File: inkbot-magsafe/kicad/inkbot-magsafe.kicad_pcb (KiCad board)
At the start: 4 copper layers, 60 x 99 mm, 70 parts, among them J1 Hirose_FH12-24S-0.5SH_1x24-1M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, J2 Molex_Pico-EZmate_78171-0003_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, J3 Coil_SolderPads, Q1 SOT-323_SC-70, U1 Raytac_MDBT50Q, U2 Texas_VQFN-RHL-20, U3 BQ25185_DLH0010A, U4 SOT-23-5, Y1 Crystal_SMD_3215-2Pin_3.2x1.5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

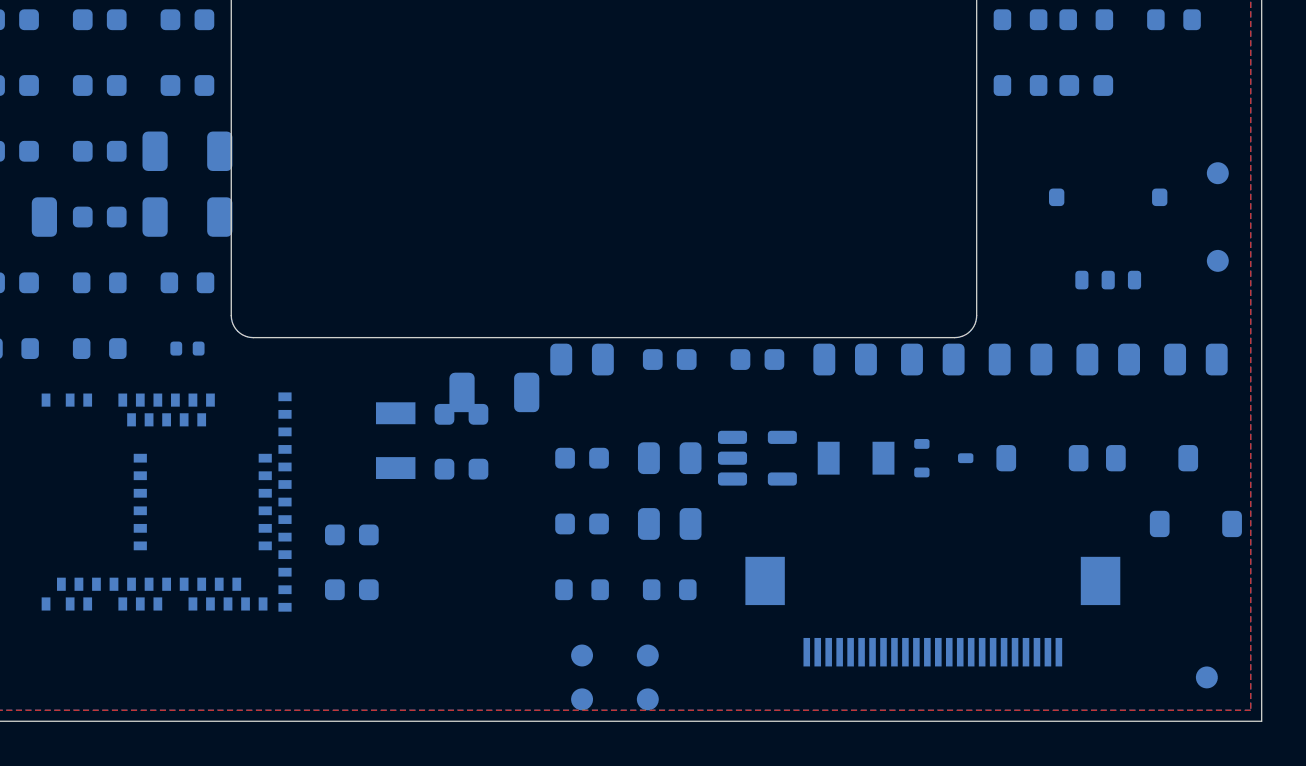
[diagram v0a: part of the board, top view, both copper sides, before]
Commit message: inkbot-magsafe: clear production placement rules
Co-authored-by: Jason Hall <imjasonh@users.noreply.github.com>
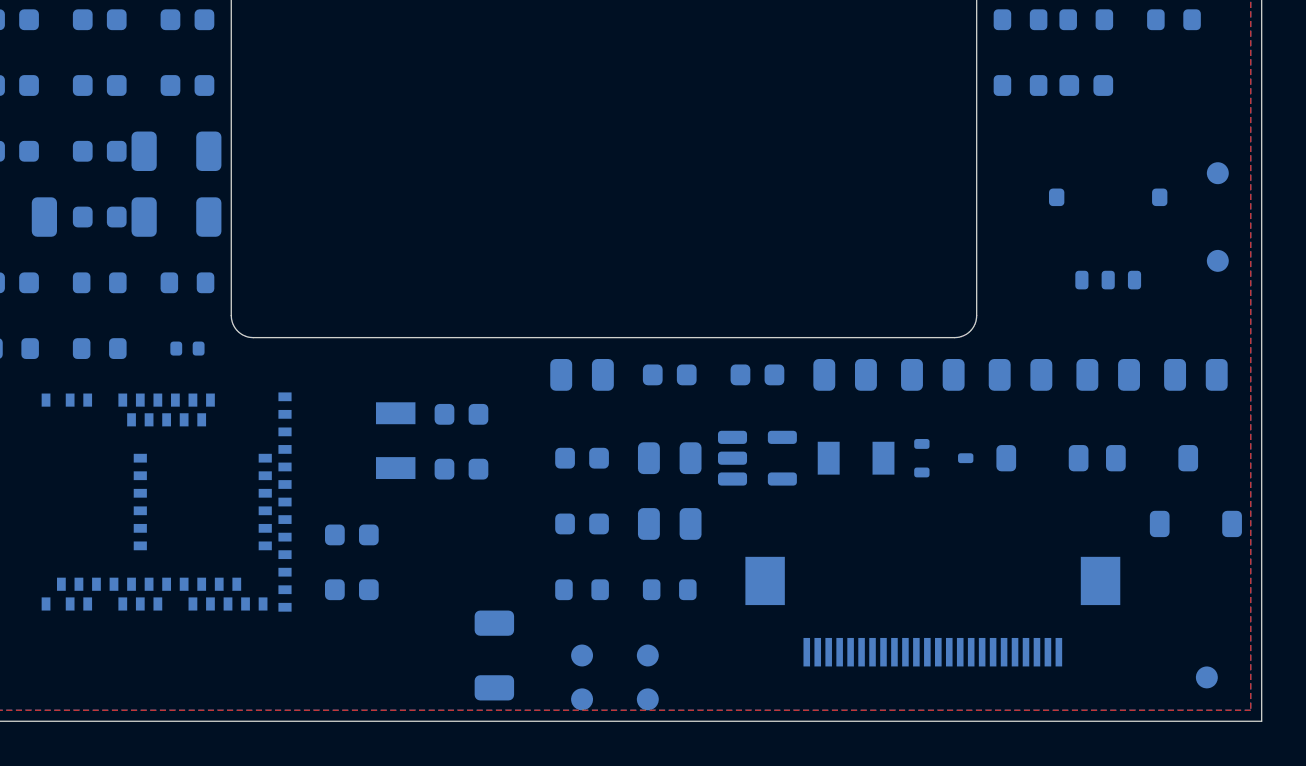
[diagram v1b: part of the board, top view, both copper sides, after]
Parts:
- moved C38 12.0 mm to (25.0, 96.0), turned to -90 degrees
- moved C28 0.70 mm to (29.0, 83.2)
- moved C29 0.70 mm to (33.0, 83.2)
- moved C30 0.70 mm to (37.0, 83.2)
- moved C31 0.70 mm to (41.0, 83.2)
- moved C32 0.70 mm to (45.0, 83.2)
- moved C33 0.70 mm to (49.0, 83.2)
- moved C34 0.70 mm to (53.0, 83.2)
- moved C35 0.70 mm to (57.0, 83.2)
- moved C12 0.50 mm to (10.5, 73.0)
- moved C15 0.50 mm to (10.5, 76.0)

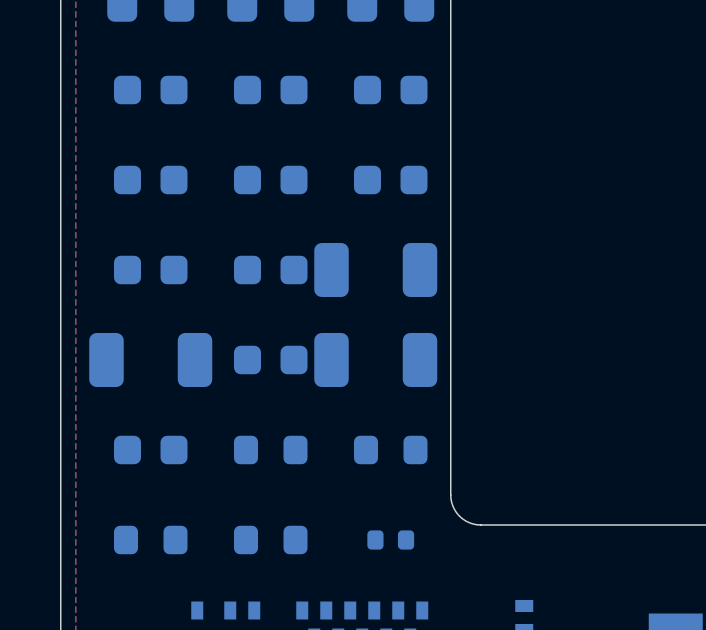
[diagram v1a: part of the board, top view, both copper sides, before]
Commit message: inkbot-magsafe: finish EVT placement clearance
Co-authored-by: Jason Hall <imjasonh@users.noreply.github.com>
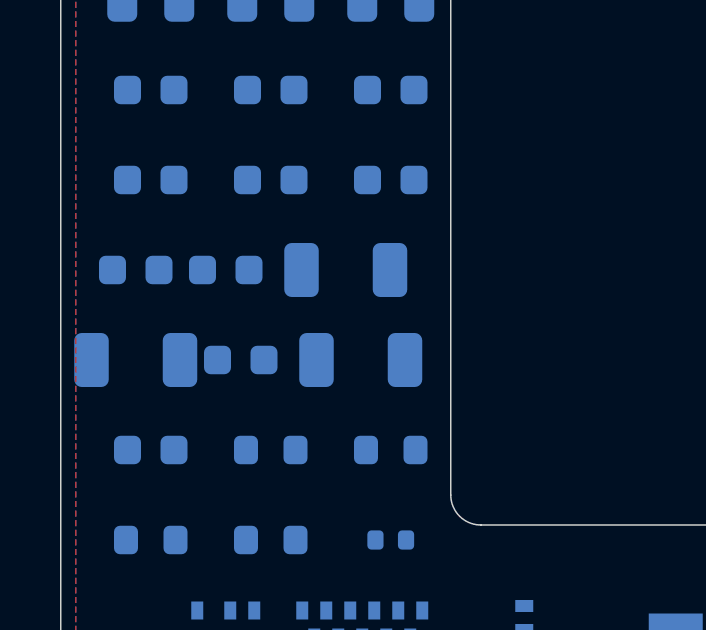
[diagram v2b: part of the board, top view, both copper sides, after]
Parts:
- moved C11 1.50 mm to (5.50, 73.0)
- moved C12 1.00 mm to (9.50, 73.0)
- moved C14 1.00 mm to (6.00, 76.0)
- moved C10 0.50 mm to (2.50, 73.0)
- moved C13 0.50 mm to (2.50, 76.0)
- moved C15 0.50 mm to (10.0, 76.0)

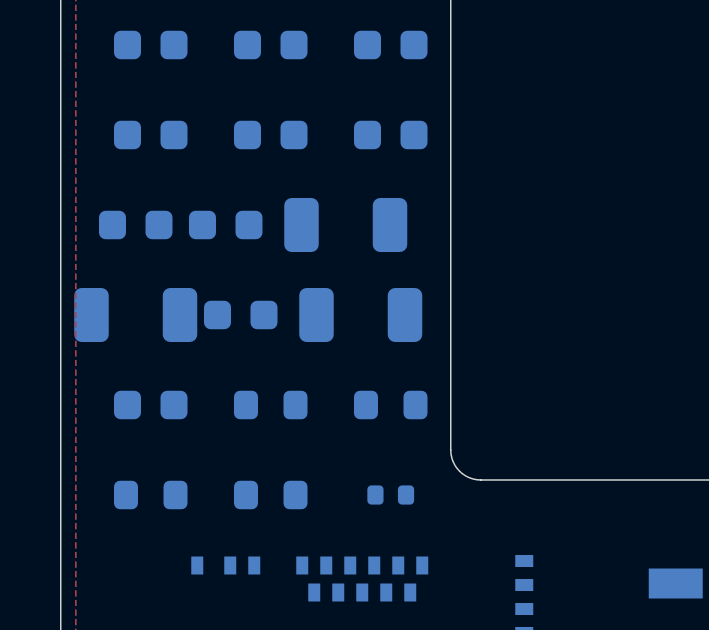
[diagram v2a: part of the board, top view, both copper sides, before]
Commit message: inkbot-magsafe: complete placed-pad contracts
Co-authored-by: Jason Hall <imjasonh@users.noreply.github.com>
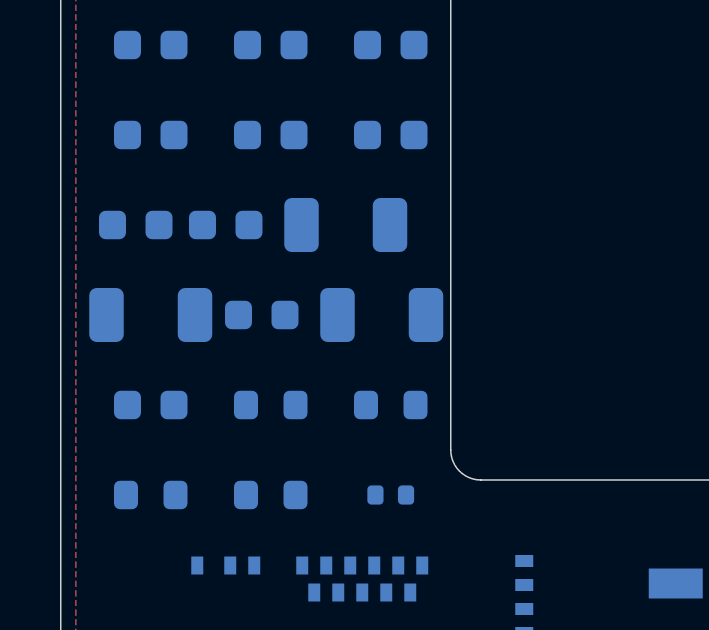
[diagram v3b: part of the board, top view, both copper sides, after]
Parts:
- moved C14 0.70 mm to (6.70, 76.0)
- moved C15 0.70 mm to (10.7, 76.0)
- moved C13 0.50 mm to (3.00, 76.0)

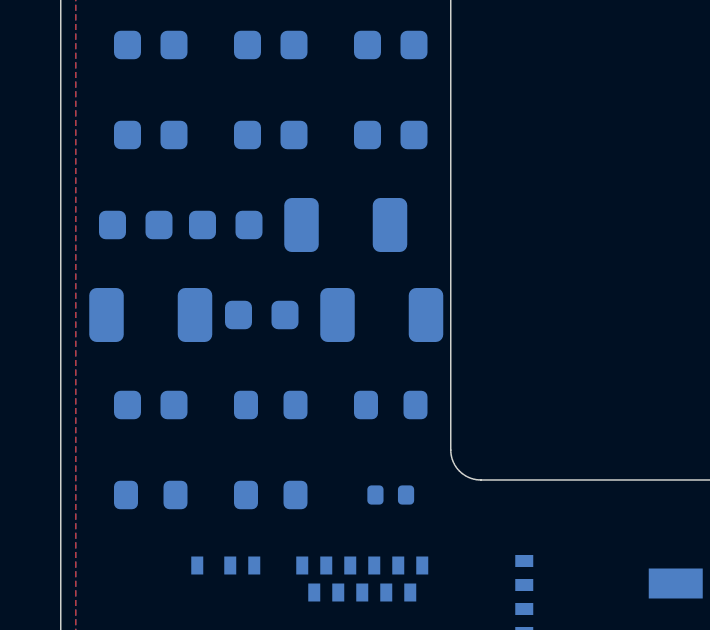
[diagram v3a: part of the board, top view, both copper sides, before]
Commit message: inkbot-magsafe: clear battery-edge placement
Co-authored-by: Jason Hall <imjasonh@users.noreply.github.com>
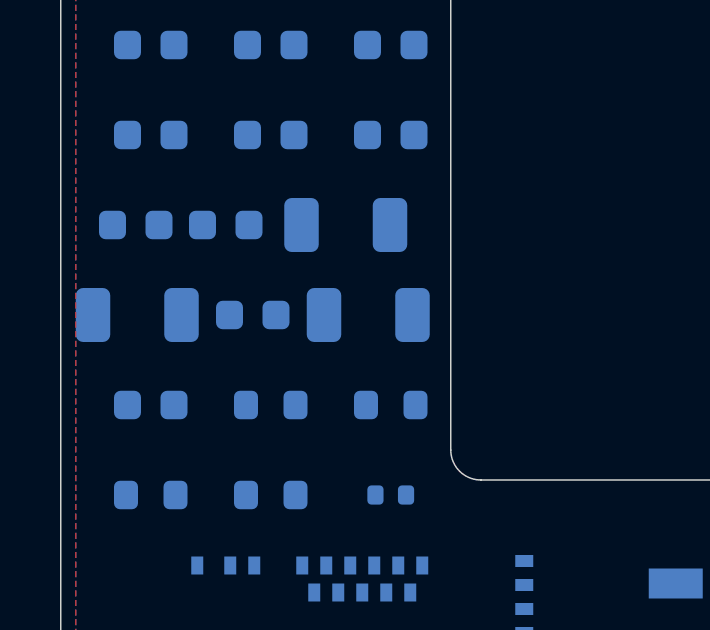
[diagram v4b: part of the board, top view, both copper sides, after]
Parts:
- moved C13 0.45 mm to (2.55, 76.0)
- moved C15 0.45 mm to (10.2, 76.0)
- moved C14 0.30 mm to (6.40, 76.0)

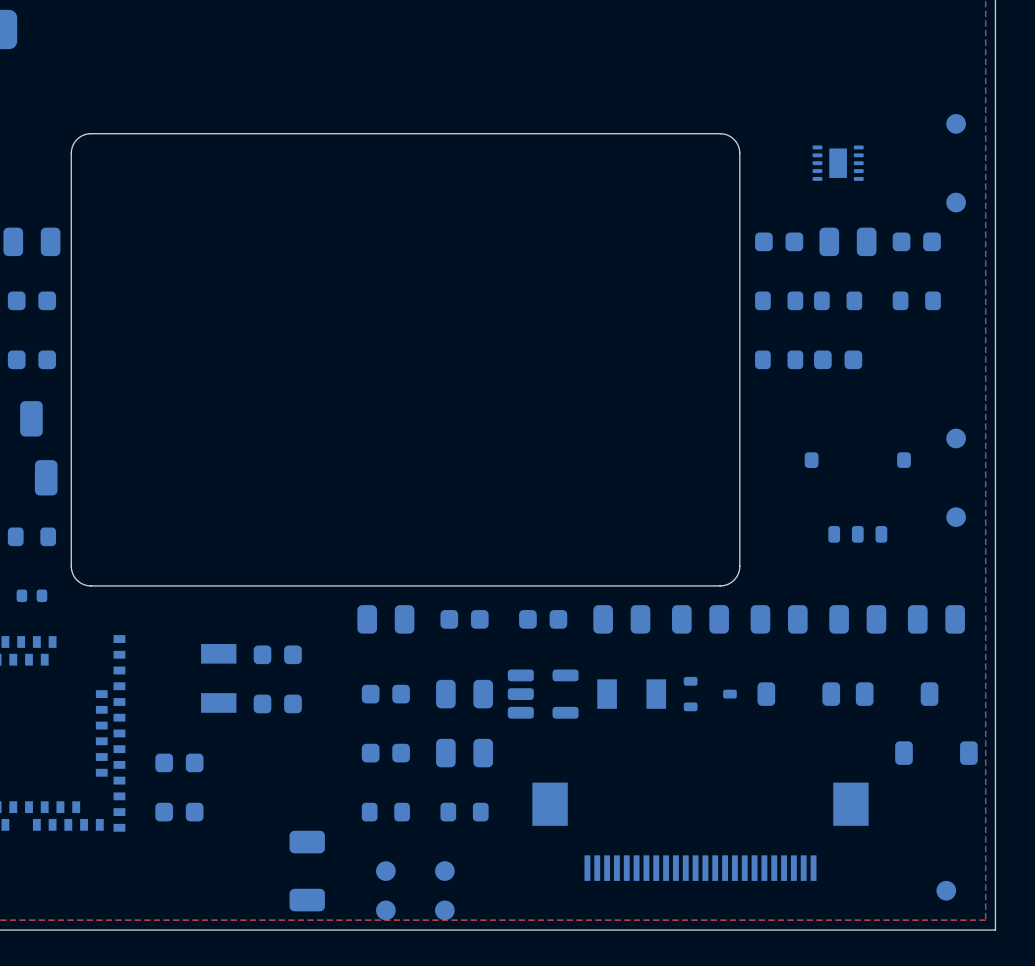
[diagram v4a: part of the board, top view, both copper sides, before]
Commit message: inkbot-magsafe: preconnect power and charge control
Co-authored-by: Jason Hall <imjasonh@users.noreply.github.com>
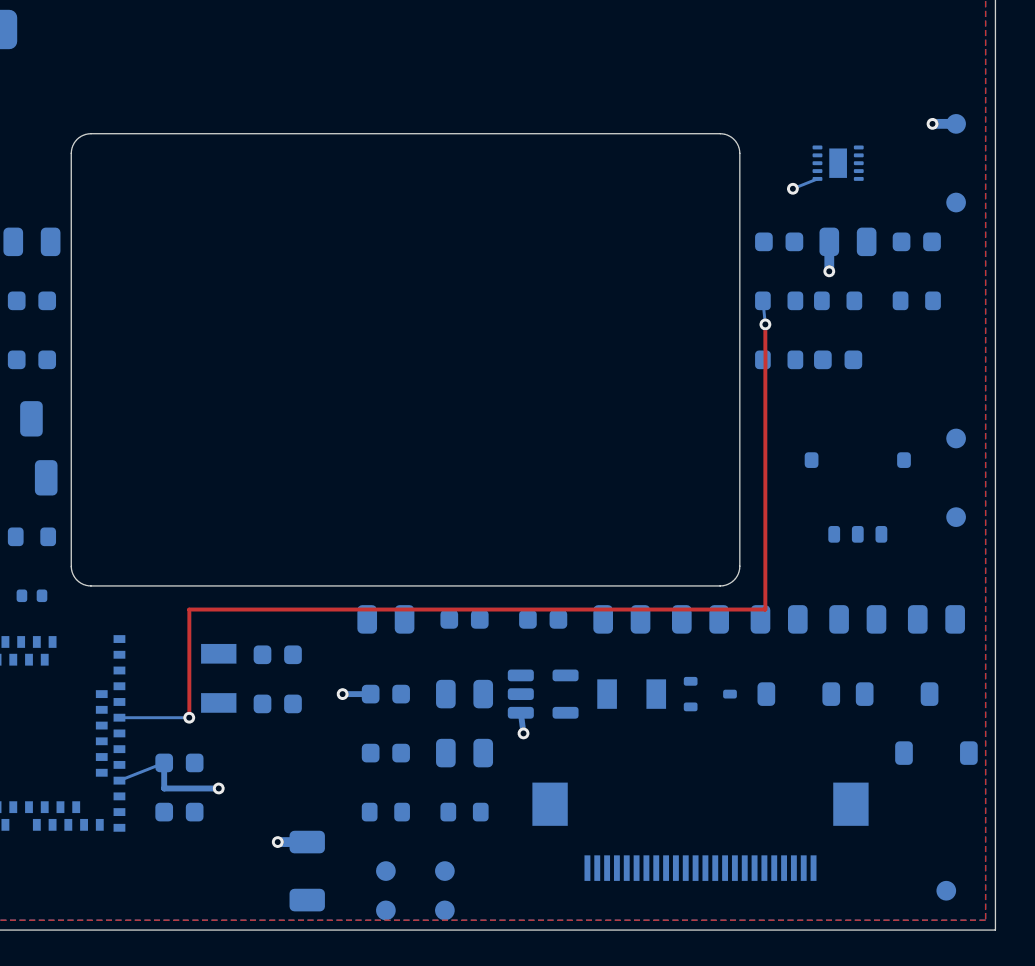
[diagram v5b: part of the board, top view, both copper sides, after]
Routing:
- net /CHG_EN_N: track 0.00 -> 54.1 mm, vias 0 -> 2
- net /SYS: track 0.00 -> 14.6 mm, vias 0 -> 7

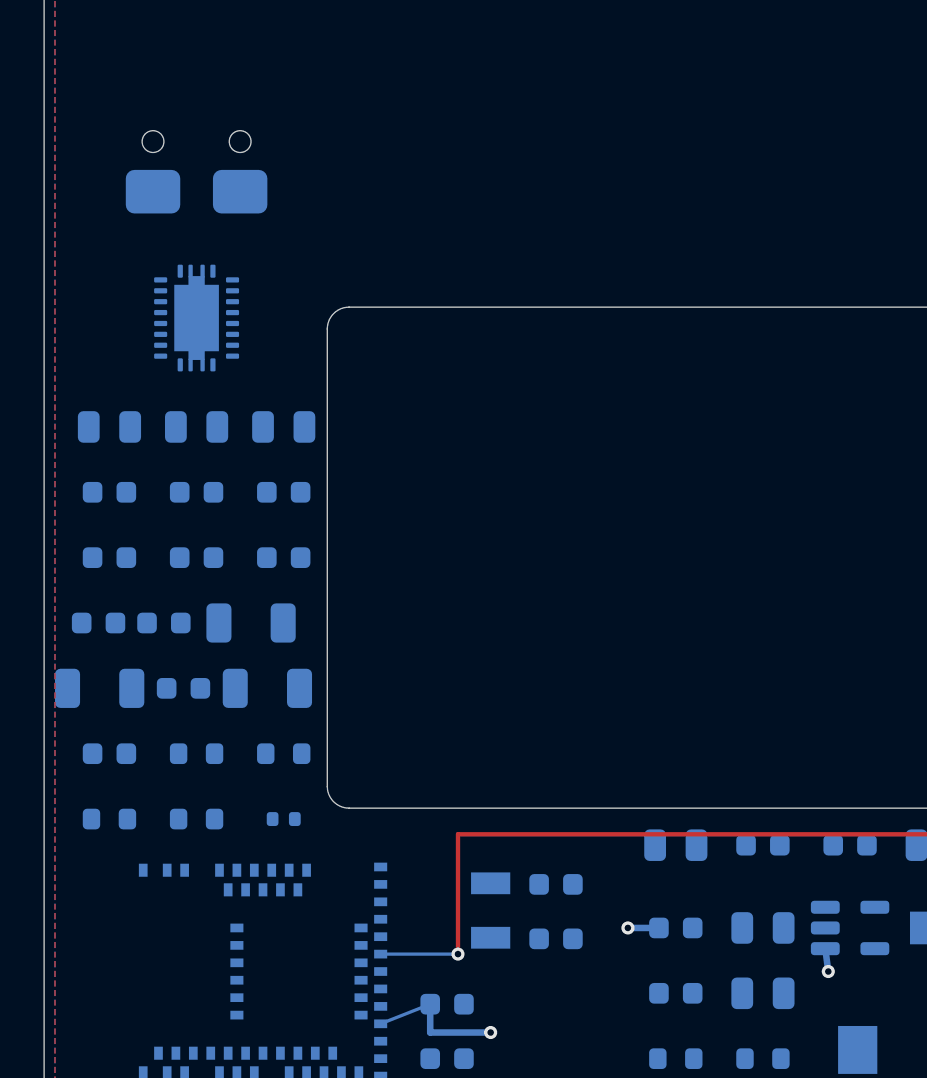
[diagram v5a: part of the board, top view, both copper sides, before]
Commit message: inkbot-magsafe: bound panel inrush and sense coil heat
Co-authored-by: Jason Hall <imjasonh@users.noreply.github.com>
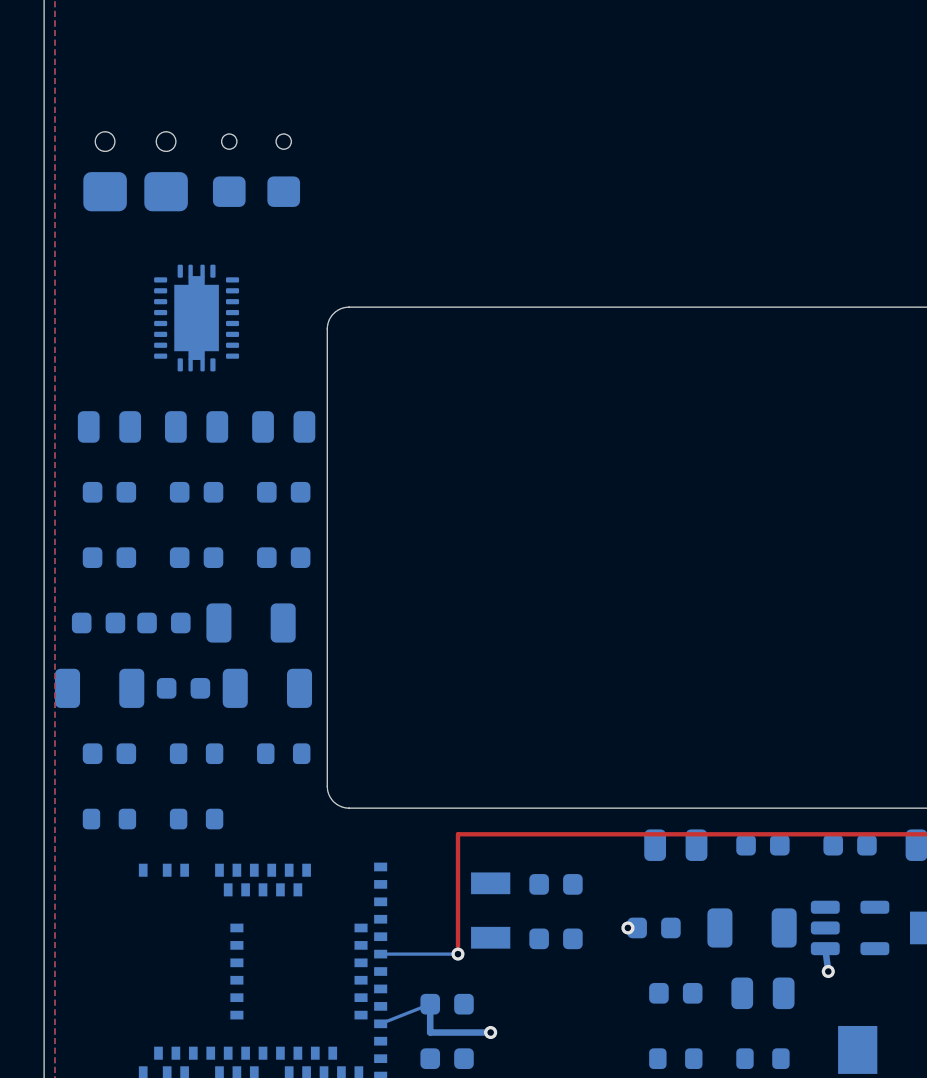
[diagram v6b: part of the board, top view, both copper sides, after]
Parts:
- removed RT2: R_0402_1005Metric, Resistor_SMD:R_0402_1005Metric
- C27: value C_0805_2012Metric -> C_1206_3216Metric; footprint Capacitor_SMD:C_0805_2012Metric -> Capacitor_SMD:C_1206_3216Metric
- moved C26 1.00 mm to (28.0, 87.0)
- moved C27 0.50 mm to (32.5, 87.0)
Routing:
- net /SYS: track 14.6 -> 13.6 mm

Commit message: inkbot-magsafe: route ground pads directly to plane
Co-authored-by: Jason Hall <imjasonh@users.noreply.github.com>
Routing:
- removed copper zone on B.Cu, net GND
- removed copper zone on F.Cu, net GND
